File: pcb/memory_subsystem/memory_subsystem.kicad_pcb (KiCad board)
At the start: 2 copper layers, 63 parts, among them J1 CLK, J2 Addr In, J3 Data In, J4 Word In, J5 Power, SW1 RUN, SW2 HLT, SW3 HLT Word, SW4 SW_DIP_x01, U1 74189, U10 74189, U11 74189, U12 74LS245, U13 74LS85, U14 74LS85, U15 74LS21, U16 74LS32, U17 74LS139, U18 74LS161, U19 74LS161, U2 74189, U20 74LS157, U21 74LS157, U22 74LS279, U23 74LS32, U24 74LS14, U3 74LS245, U4 74189, U5 74189, U6 74LS245, U7 74189, U8 74189, U9 74LS245

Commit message: Tracks finished
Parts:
- removed J4: Word In, Connector_PinHeader_2.54mm:PinHeader_1x08_P2.54mm_Vertical
- removed RN1, RN2: R_Network08, Resistor_THT:R_Array_SIP9
- added J6: Data Out, Connector_PinHeader_2.54mm:PinHeader_1x08_P2.54mm_Vertical, F.Cu at (281.2, 58.9)
- added R10: R, Resistor_SMD:R_0805_2012Metric_Pad1.20x1.40mm_HandSolder, F.Cu at (174.6, 150.6)
- added R11: R, Resistor_SMD:R_0805_2012Metric_Pad1.20x1.40mm_HandSolder, F.Cu at (172.1, 150.6)
- added R12: R, Resistor_SMD:R_0805_2012Metric_Pad1.20x1.40mm_HandSolder, F.Cu at (169.5, 150.6)
- added R13: R, Resistor_SMD:R_0805_2012Metric_Pad1.20x1.40mm_HandSolder, F.Cu at (129.3, 140.2)
- added R14: R, Resistor_SMD:R_0805_2012Metric_Pad1.20x1.40mm_HandSolder, F.Cu at (131.8, 140.2)
- added R15: R, Resistor_SMD:R_0805_2012Metric_Pad1.20x1.40mm_HandSolder, F.Cu at (134.4, 140.2)
- added R16: R, Resistor_SMD:R_0805_2012Metric_Pad1.20x1.40mm_HandSolder, F.Cu at (136.9, 140.2)
- added R17: R, Resistor_SMD:R_0805_2012Metric_Pad1.20x1.40mm_HandSolder, F.Cu at (139.4, 140.2)
- added R18: R, Resistor_SMD:R_0805_2012Metric_Pad1.20x1.40mm_HandSolder, F.Cu at (142.0, 140.2)
- added R19: R, Resistor_SMD:R_0805_2012Metric_Pad1.20x1.40mm_HandSolder, F.Cu at (144.5, 140.2)
- added R20: R, Resistor_SMD:R_0805_2012Metric_Pad1.20x1.40mm_HandSolder, F.Cu at (147.1, 140.2)
- added R5: R, Resistor_SMD:R_0805_2012Metric_Pad1.20x1.40mm_HandSolder, F.Cu at (187.3, 150.6)
- added R6: R, Resistor_SMD:R_0805_2012Metric_Pad1.20x1.40mm_HandSolder, F.Cu at (184.8, 150.6)
- added R7: R, Resistor_SMD:R_0805_2012Metric_Pad1.20x1.40mm_HandSolder, F.Cu at (182.2, 150.6)
- added R8: R, Resistor_SMD:R_0805_2012Metric_Pad1.20x1.40mm_HandSolder, F.Cu at (179.7, 150.6)
- added R9: R, Resistor_SMD:R_0805_2012Metric_Pad1.20x1.40mm_HandSolder, F.Cu at (177.2, 150.6)
- SW3: footprint Connector_PinHeader_2.54mm:PinHeader_1x16_P2.54mm_Vertical -> Button_Switch_THT:SW_DIP_SPSTx08_Slide_9.78x22.5mm_W7.62mm_P2.54mm
- SW4: value SW_DIP_x01 -> W_EN
- U1, U10, U11, U2, U4, U5, U7, U8: value 74189 -> ~
- moved J5 282.2 mm to (278.4, 22.4), turned to 90 degrees
- moved C6 186.4 mm to (246.4, 35.1)
- moved J3 182.7 mm to (187.3, 146.9), turned to -90 degrees
- moved SW3 165.9 mm to (147.1, 144.0), turned to -90 degrees
- moved C4 157.1 mm to (215.9, 35.1)
- moved C3 151.6 mm to (246.4, 65.5)
- moved U13 121.8 mm to (144.8, 109.2), turned to 90 degrees
- moved C23 114.1 mm to (145.8, 79.2), turned to 180 degrees
- moved C1 112.0 mm to (215.9, 65.5)
- moved U15 111.4 mm to (144.8, 130.8), turned to 90 degrees
- moved C24 108.6 mm to (145.8, 99.6), turned to 180 degrees
- moved U14 106.4 mm to (144.8, 88.9), turned to 90 degrees
- moved C12 104.7 mm to (246.4, 96.0)
- moved U22 89.9 mm to (114.0, 130.8), turned to 90 degrees
- moved C2 88.4 mm to (185.4, 65.5)
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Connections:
- J3 pad 2: /Win1 -> /Din1
- U16 pad 1: /Address Selector/CS1 -> /Address Selector/CS0
- U20 pad 1: /Address Selector/CS1 -> /Address Selector/R/W
- U21 pad 1: /Address Selector/CS1 -> /Address Selector/R/W
- U9 pad 11: /Out7 -> /Ram Unit3/Out7
- U9 pad 12: /Out6 -> /Ram Unit3/Out6
- U9 pad 13: /Out5 -> /Ram Unit3/Out5
- U9 pad 14: /Out4 -> /Ram Unit3/Out4
- U9 pad 15: /Out3 -> /Ram Unit3/Out3
- U9 pad 16: /Out2 -> /Ram Unit3/Out2
- U9 pad 17: /Out1 -> /Ram Unit3/Out1
- U9 pad 18: /Out0 -> /Ram Unit3/Out0
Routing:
- net +5V: track 0.00 -> 1121.5 mm, vias 0 -> 8
- net /Address Selector/SAddr1: track 0.00 -> 414.1 mm, vias 0 -> 14
- net /Address Selector/SAddr3: track 0.00 -> 400.1 mm, vias 0 -> 13
- net /Address Selector/SAddr2: track 0.00 -> 395.5 mm, vias 0 -> 13
- net /Din5: track 0.00 -> 393.6 mm, vias 0 -> 9
- net /Din4: track 0.00 -> 378.7 mm, vias 0 -> 9
- net /Din6: track 0.00 -> 373.2 mm, vias 0 -> 9
- net /Address Selector/SAddr0: track 0.00 -> 366.0 mm, vias 0 -> 14
- net /Din7: track 0.00 -> 360.5 mm, vias 0 -> 9
- net /Din2: track 0.00 -> 225.2 mm, vias 0 -> 9
- net /Din3: track 0.00 -> 211.3 mm, vias 0 -> 5
- net /Out0: track 0.00 -> 210.7 mm, vias 0 -> 5
- net /Address Selector/OE2: track 0.00 -> 205.5 mm, vias 0 -> 4
- net /Din1: track 0.00 -> 205.3 mm, vias 0 -> 5
- net /Control Logic/RAM_WE: track 0.00 -> 199.2 mm
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
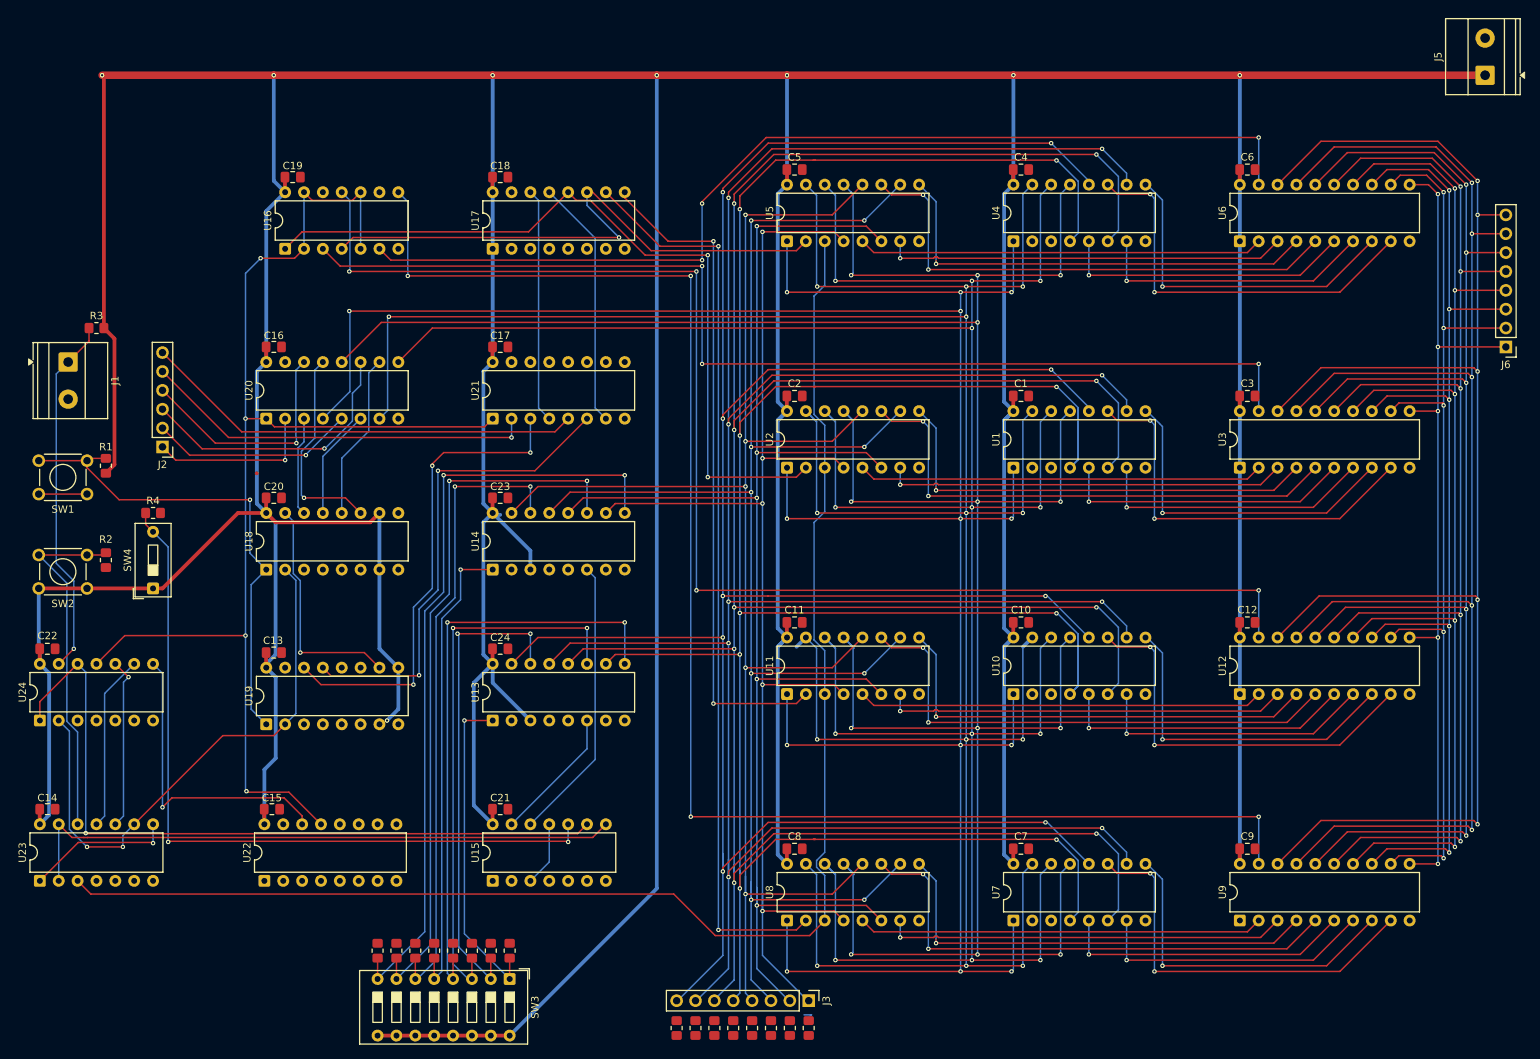
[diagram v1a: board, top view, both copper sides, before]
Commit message: Finished mem subsystem pcb
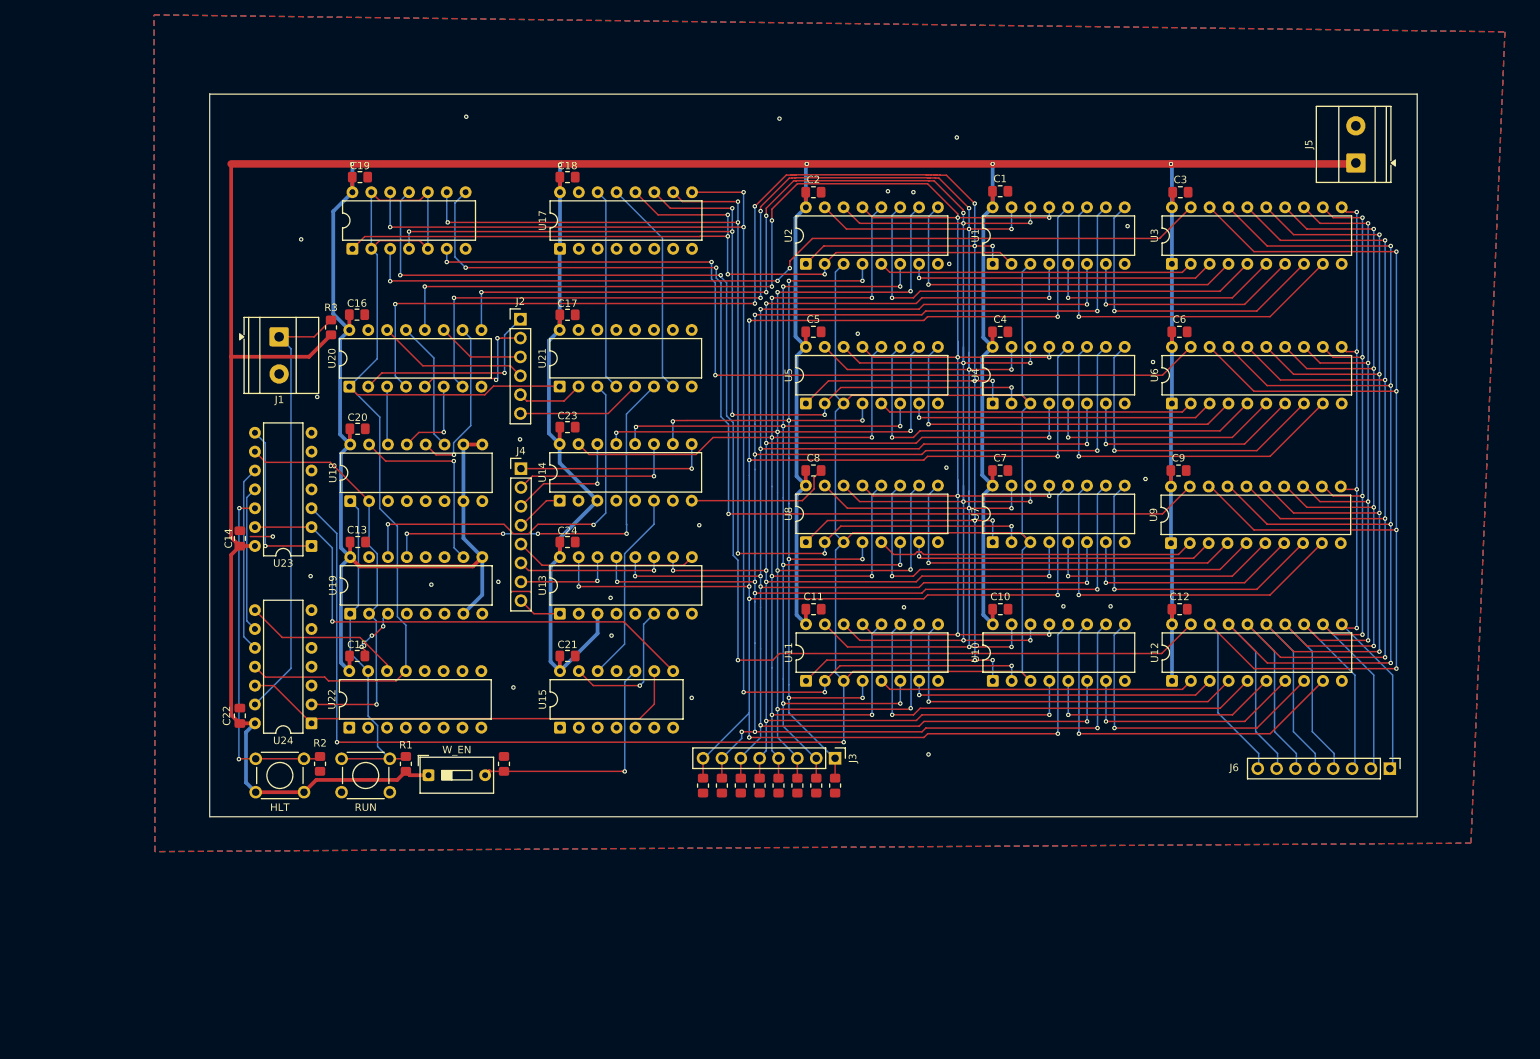
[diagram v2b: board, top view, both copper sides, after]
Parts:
- removed R13, R14, R15, R16, R17, R18, R19, R20: R, Resistor_SMD:R_0805_2012Metric_Pad1.20x1.40mm_HandSolder
- removed SW3: HLT Word, Button_Switch_THT:SW_DIP_SPSTx08_Slide_9.78x22.5mm_W7.62mm_P2.54mm
- added J4: Word In, Connector_PinHeader_2.54mm:PinHeader_1x08_P2.54mm_Vertical, F.Cu at (148.6, 75.3)
- moved J6 58.9 mm to (265.6, 115.7), turned to -90 degrees
- moved R4 58.1 mm to (146.3, 115.1), turned to 90 degrees
- moved U23 58.1 mm to (120.4, 85.7), turned to 180 degrees
- moved RUN 57.2 mm to (130.9, 118.9)
- moved R1 56.9 mm to (133.1, 115.1)
- moved C9 51.8 mm to (237.1, 75.6)
- moved U9 51.6 mm to (236.1, 85.3)
- moved J2 51.2 mm to (148.5, 55.2), turned to 0 degrees
- moved C7 51.0 mm to (213.1, 75.6)
- moved U7 51.0 mm to (212.1, 85.2)
- moved U8 51.0 mm to (186.9, 85.2)
- moved C8 51.0 mm to (188.0, 75.6)
- moved W_EN 44.8 mm to (136.1, 116.6), turned to 0 degrees
- moved C14 44.7 mm to (110.7, 84.7), turned to -90 degrees
- moved HLT 40.1 mm to (119.4, 118.9)
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- renumbered SW2 to HLT, SW1 to RUN, SW4 to W_EN
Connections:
- U9 pad 11: /Ram Unit3/Out7 -> /Out7
- U9 pad 12: /Ram Unit3/Out6 -> /Out6
- U9 pad 13: /Ram Unit3/Out5 -> /Out5
- U9 pad 14: /Ram Unit3/Out4 -> /Out4
- U9 pad 15: /Ram Unit3/Out3 -> /Out3
- U9 pad 16: /Ram Unit3/Out2 -> /Out2
- U9 pad 17: /Ram Unit3/Out1 -> /Out1
- U9 pad 18: /Ram Unit3/Out0 -> /Out0
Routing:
- net +5V: track 1121.5 -> 731.8 mm, vias 8 -> 5
- net /Address Selector/SAddr3: track 400.1 -> 260.4 mm, vias 13 -> 11
- net /Address Selector/SAddr2: track 395.5 -> 259.3 mm, vias 13 -> 12
- net /Address Selector/SAddr1: track 414.1 -> 278.5 mm, vias 14 -> 12
- net /Din4: track 378.7 -> 250.6 mm, vias 9 -> 10
- net /Din5: track 393.6 -> 282.5 mm, vias 9 -> 10
- net /Control Logic/RAM_WE: track 199.2 -> 305.6 mm, vias 0 -> 2
- net /Address Selector/SAddr0: track 366.0 -> 284.8 mm, vias 14 -> 12
- net /Win0: track 103.8 -> 26.3 mm, vias 2 -> 1
- net /Address Selector/CS3: track 90.3 -> 167.0 mm, vias 2 -> 6
- net /Win1: track 95.7 -> 22.9 mm, vias 2 -> 1
- net /Word Comparator/word_EN: track 101.8 -> 33.1 mm, vias 2 -> 1
- net /Win2: track 85.2 -> 16.9 mm, vias 2 -> 1
- net /Address Selector/OE2: track 205.5 -> 142.6 mm, vias 4 -> 3
- net /Win3: track 63.7 -> 6.58 mm, vias 1 -> 0
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- added copper zone on B.Cu, net GND
- added copper zone on F.Cu, net GND
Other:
- board outline added: 162.6 x 97.3 mm
